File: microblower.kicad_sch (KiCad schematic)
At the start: 18 parts, among them Q1 2N7000, U1 NE555P, U2 L293D, U3 LM78L05_TO92, U4 TL072

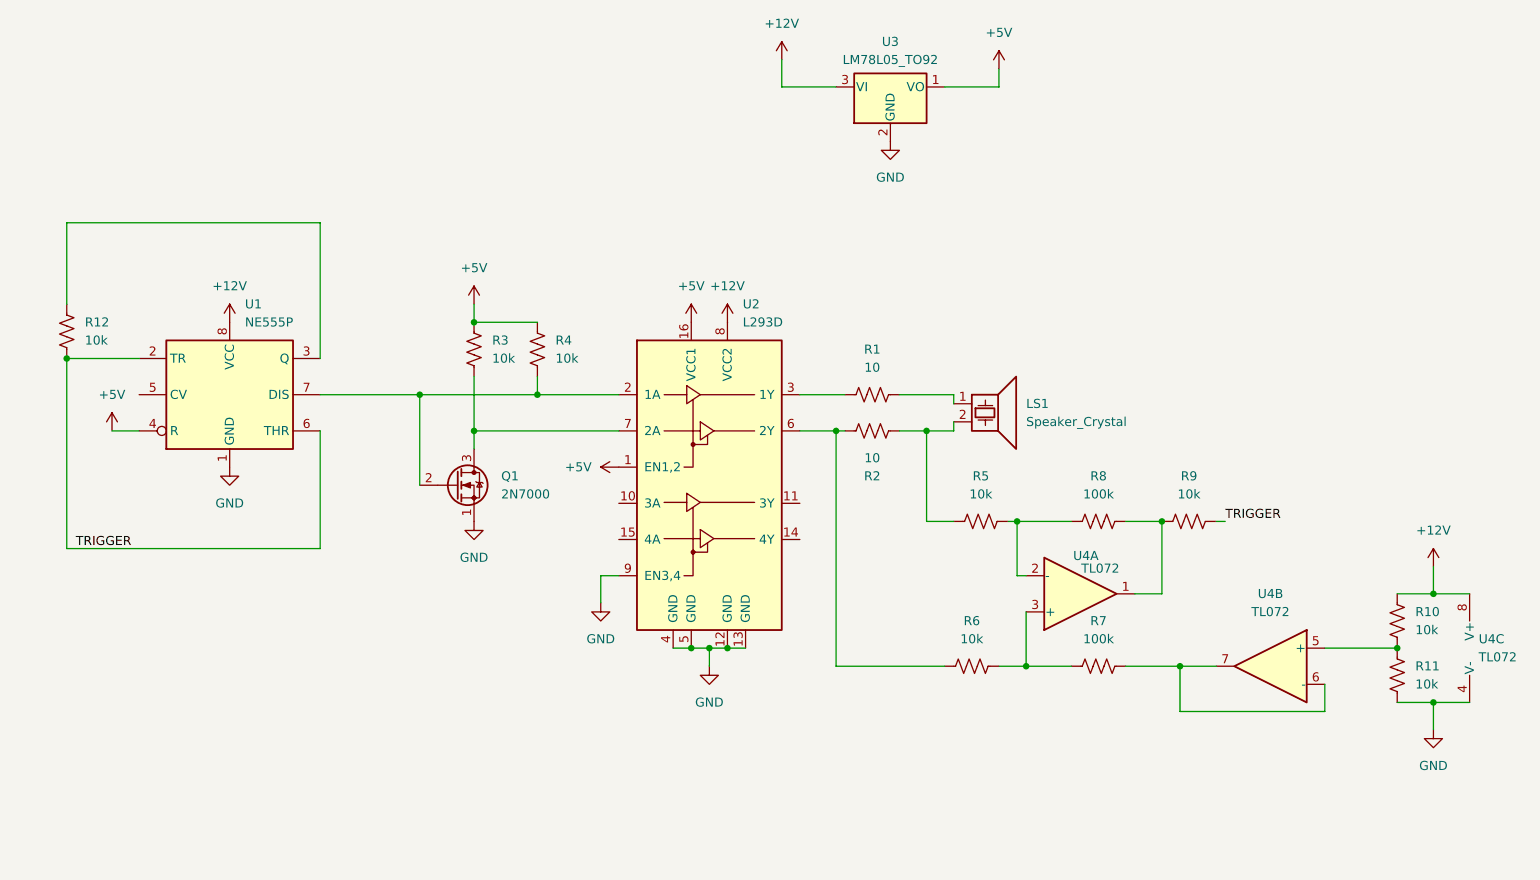
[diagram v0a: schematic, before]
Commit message: Tried basic pierce oscillator
Didn't have enough phase shift
I think the feedback resistor is misplaced
No way to drive the second side of the invertere
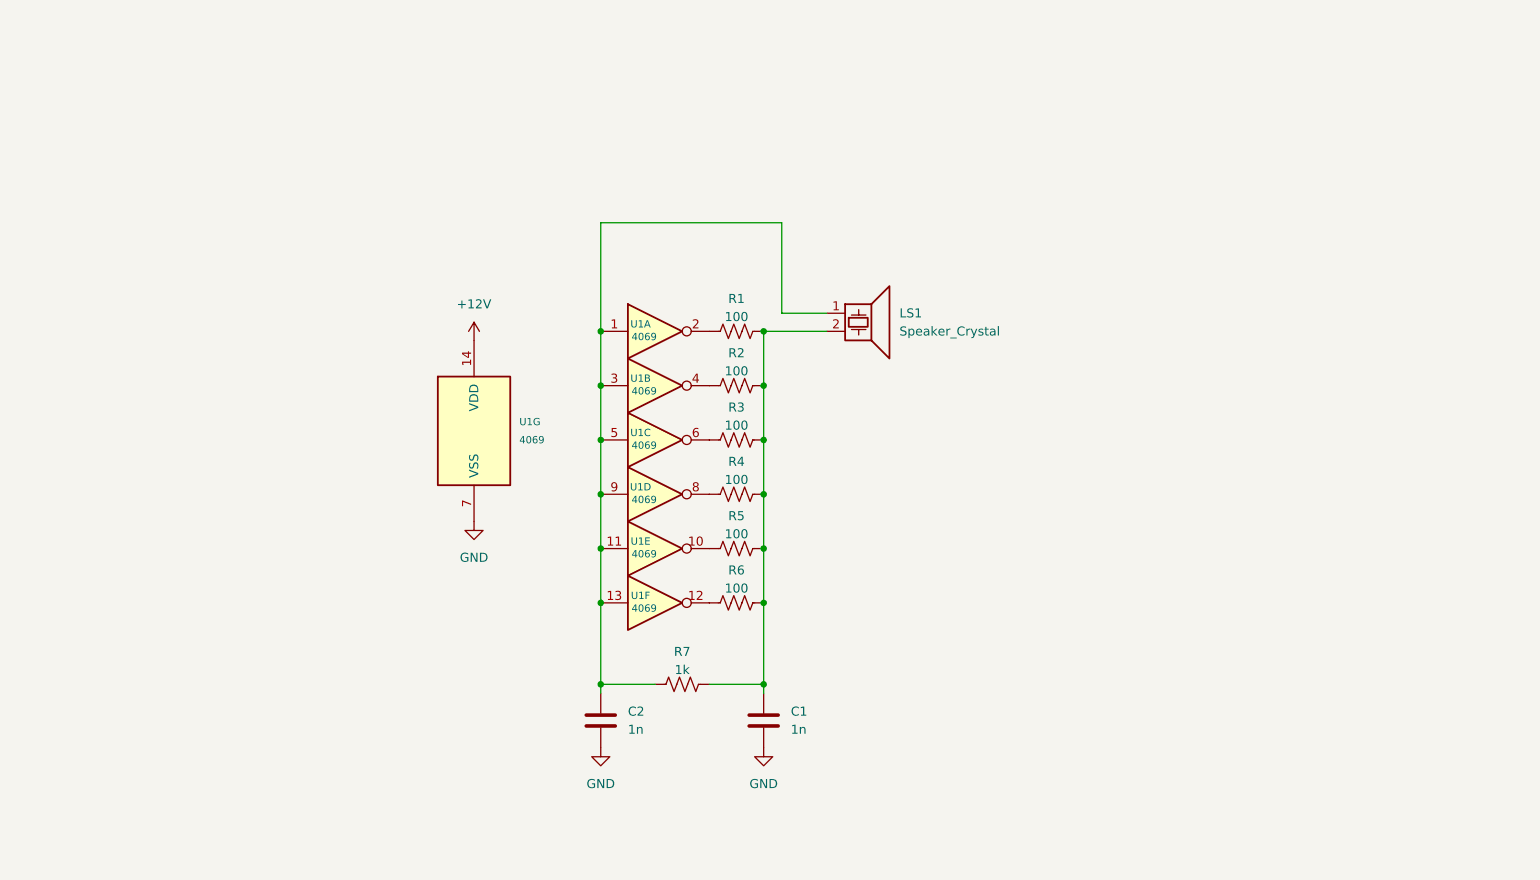
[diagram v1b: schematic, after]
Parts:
- removed Q1: 2N7000, Package_TO_SOT_THT:TO-92_Inline, symbol Transistor_FET:2N7000
- removed R10, R11, R12, R9: 10k, Resistor_THT:R_Axial_DIN0204_L3.6mm_D1.6mm_P7.62mm_Horizontal, symbol Device:R_US
- removed R8: 100k, Resistor_THT:R_Axial_DIN0204_L3.6mm_D1.6mm_P7.62mm_Horizontal, symbol Device:R_US
- removed U1: NE555P, Package_DIP:DIP-8_W7.62mm, symbol Timer:NE555P
- removed U2: L293D, Package_DIP:DIP-16_W7.62mm, symbol Driver_Motor:L293D
- removed U3: LM78L05_TO92, Package_TO_SOT_THT:TO-92_Inline, symbol Regulator_Linear:LM78L05_TO92
- removed U4: TL072, Package_DIP:DIP-8_W7.62mm, symbol Amplifier_Operational:TL072
- added C1, C2: 1n, Capacitor_THT:C_Disc_D3.0mm_W2.0mm_P2.50mm, symbol Device:C
- added U1: 4069, Package_DIP:DIP-14_W7.62mm, symbol 4xxx:4069
- R1, R2: value 10 -> 100
- R3, R4, R5, R6: value 10k -> 100
- R7: value 100k -> 1k
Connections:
- net +12V: now also U1.14 (VDD)
- net GND: now also C1.2, C2.2, U1.7 (VSS)
- net at R2.1: now also U1.4; no longer R6.1
- net at R7.1: now also LS1.1, C2.1, U1.1, U1.11, U1.13, U1.3, U1.5, U1.9; no longer R6.2
- net at R5.2: now also LS1.2, R1.2, R2.2, R3.2, R4.2, R6.2, R7.2, C1.1
- net at R1.1: now also U1.2
- net +5V: no longer names the net of R4.1
- net +5V: now also U1.8; no longer R3.1
- new net: R3.1, U1.6
- new net: R5.1, U1.10
- new net: R6.1, U1.12
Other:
- moved on the sheet: LS1

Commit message: Switched to relaxation oscillator
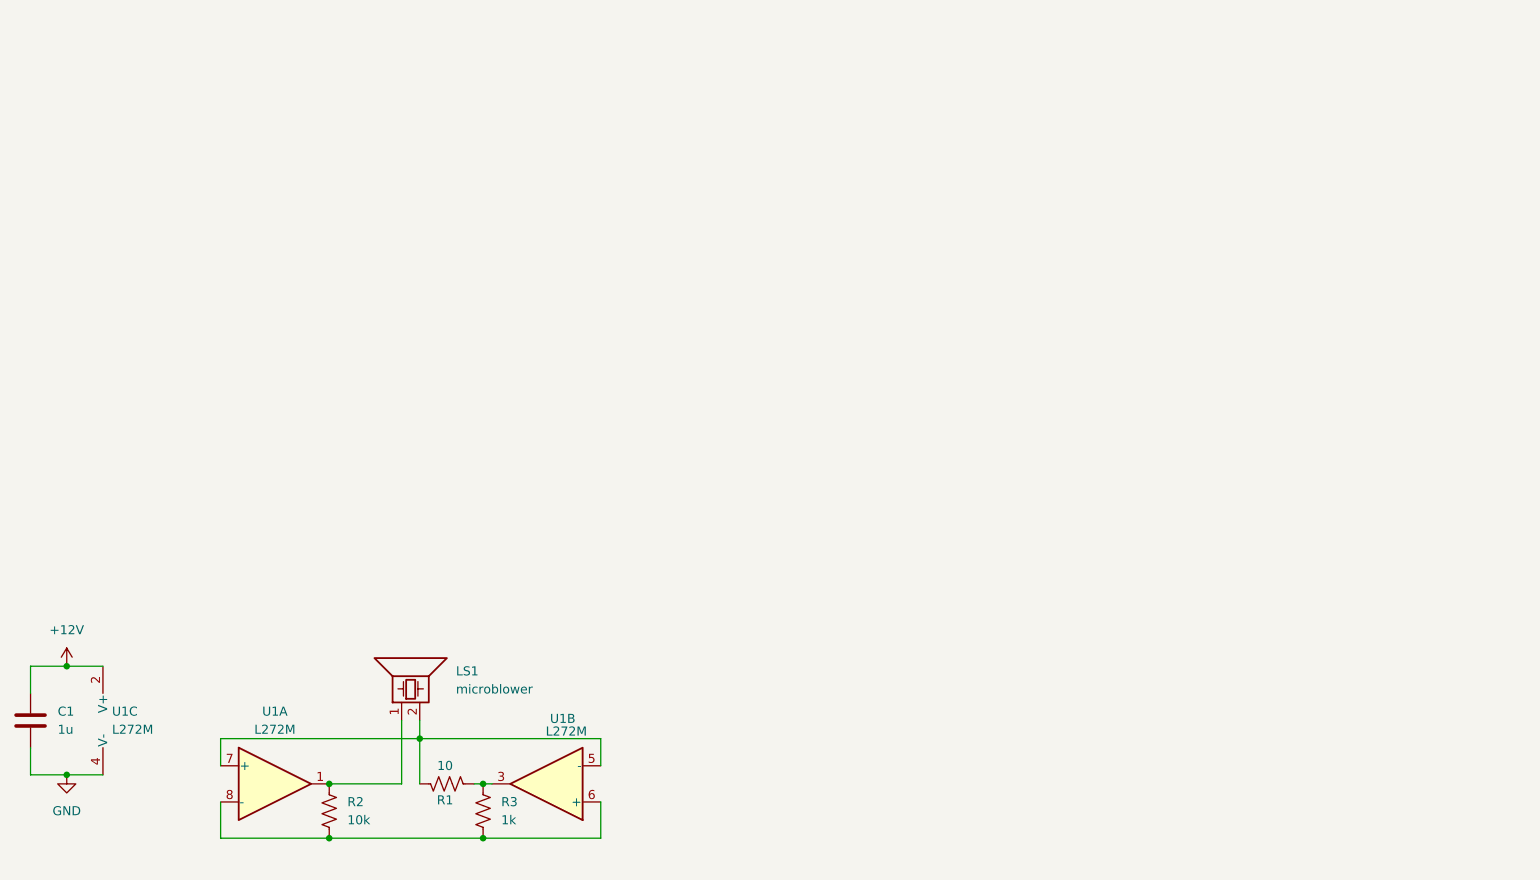
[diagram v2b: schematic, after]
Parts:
- removed C2: 1n, Capacitor_THT:C_Disc_D3.0mm_W2.0mm_P2.50mm, symbol Device:C
- removed R4, R5, R6: 100, Resistor_THT:R_Axial_DIN0204_L3.6mm_D1.6mm_P7.62mm_Horizontal, symbol Device:R_US
- removed R7: 1k, Resistor_THT:R_Axial_DIN0204_L3.6mm_D1.6mm_P7.62mm_Horizontal, symbol Device:R_US
- removed U1: 4069, Package_DIP:DIP-14_W7.62mm, symbol 4xxx:4069
- added U1: L272M, Package_DIP:DIP-8_W7.62mm_LongPads, symbol Amplifier_Operational:L272M
- C1: value 1n -> 1u; footprint Capacitor_THT:C_Disc_D3.0mm_W2.0mm_P2.50mm -> Capacitor_THT:C_Disc_D4.7mm_W2.5mm_P5.00mm
- LS1: value Speaker_Crystal -> microblower
- R1: value 100 -> 10
- R2: value 100 -> 10k
- R3: value 100 -> 1k
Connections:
- net +12V: now also C1.1, U1.2 (V+)
- net GND: now also U1.4 (V-)
- net at LS1.1: now also R2.1, U1.1
- net at R3.1: now also R1.1, U1.3
- new net: LS1.2, R1.2, U1.5 (-), U1.7 (+)
- new net: R2.2, R3.2, U1.6 (+), U1.8 (-)
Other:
- moved on the sheet: LS1

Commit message: Settled on design for microblower
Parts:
- removed U1: L272M, Package_DIP:DIP-8_W7.62mm_LongPads, symbol Amplifier_Operational:L272M
- added C2, C3: 1u, Capacitor_THT:C_Disc_D4.7mm_W2.5mm_P5.00mm, symbol Device:C
- added C4: 100u, symbol Device:C_Polarized_US
- added Q1: 2N7000, Package_TO_SOT_THT:TO-92L_Inline_Wide, symbol Transistor_FET:2N7000
- added RV1: 5k, Potentiometer_THT:Potentiometer_Bourns_3266Y_Vertical, symbol Device:R_Potentiometer_Trim_US
- added U1: NE555P, Package_DIP:DIP-8_W7.62mm, symbol Timer:NE555P
- added U2: L293, Package_DIP:DIP-16_W7.62mm, symbol Driver_Motor:L293
- added U3: L78L05_TO92, Package_TO_SOT_THT:TO-92L_Inline_Wide, symbol Regulator_Linear:L78L05_TO92
- C1: value 1u -> 1n
- R1: value 10 -> 10k; footprint Resistor_THT:R_Axial_DIN0204_L3.6mm_D1.6mm_P7.62mm_Horizontal -> Resistor_THT:R_Axial_DIN0207_L6.3mm_D2.5mm_P2.54mm_Vertical
- R2: footprint Resistor_THT:R_Axial_DIN0204_L3.6mm_D1.6mm_P7.62mm_Horizontal -> Resistor_THT:R_Axial_DIN0207_L6.3mm_D2.5mm_P15.24mm_Horizontal
- R3: value 1k -> 22k; footprint Resistor_THT:R_Axial_DIN0204_L3.6mm_D1.6mm_P7.62mm_Horizontal -> (none)
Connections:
- net +12V: now also C2.1, C4.1, U2.8 (VCC2), U3.3 (VI); no longer C1.1
- net GND: now also C2.2, C3.2, C4.2, Q1.1 (S), U1.1 (GND), U2.12 (GND), U2.13 (GND), U2.4 (GND), U2.5 (GND), U3.2 (GND)
- net at R3.1: now also U1.3 (Q); no longer R1.1
- net at R1.2: now also Q1.2 (G), U1.7 (DIS), U2.10 (3A); no longer LS1.2
- net at R3.2: now also RV1.1; no longer R2.2
- net at LS1.1: now also U2.11 (3Y); no longer R2.1
- new net: C1.1, RV1.2, RV1.3, U1.2 (TR), U1.6 (THR)
- new net: LS1.2, U2.14 (4Y)
- new net: Q1.3 (D), R2.2, U2.15 (4A)
- new net +5V: C3.1, R1.1, R2.1, U1.4 (R), U1.8 (VCC), U2.16 (VCC1), U2.9 (EN3,4), U3.1 (VO)
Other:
- note added: "This is supplied from 5V because it's not as voltage-independent as would be expected"
- moved on the sheet: LS1
